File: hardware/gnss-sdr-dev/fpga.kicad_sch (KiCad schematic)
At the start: 31 parts, among them J501 JTAG, J502 LA, U501 LFE5U-25F-6BG256, U502 W25Q128JVSIQ

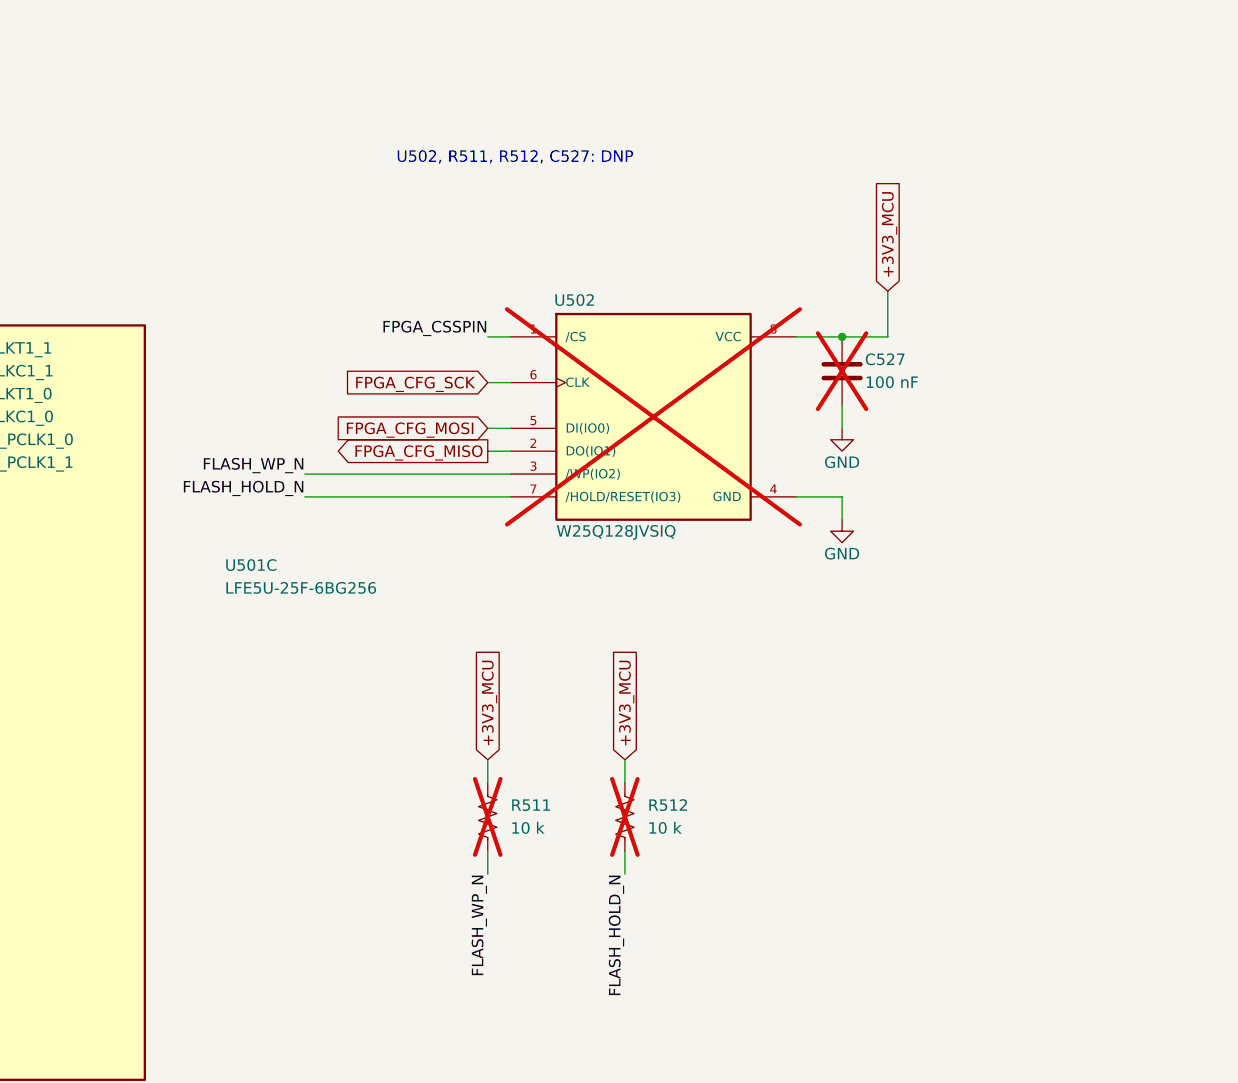
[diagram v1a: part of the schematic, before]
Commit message: hardware(gnss-sdr-dev): U502 becomes the WLCSP W25Q128JVYIQ the P4's boot flash uses, turned 180 deg and routed; the P4 cluster's wiring ripped up for hand routing
P4 rip-up (owner: "rip up the p4 wiring and vias. I'll relocate a bit and do the wiring there by hand"):
- Removed every track and via of the P4's own nets inside the cluster box (124.14, 130.34)-(142.14, 158.23),
  except J5 and R21, plus the dead-end stubs that left outside the box: 953 items.
- Kept the RF section's copper and nets with no pad on a cluster part (VSYS, the USB-C #1 VBUS, J5 CC2).
- VIN from FL401.2 to C402 had looped through the box. It is rerouted locally.

U502, the FPGA configuration flash (DNP: the P4 loads the FPGA):
- Schematic: the W25Q128JVSIQ (SOIC-8) becomes the W25Q128JVYIQ (24-ball WLCSP), the same part and footprint as U7.
  - Same symbol UUID, so the footprint stays linked. Same nets.
  - The 16 unused balls carry no-connect flags.
  - C527 is unchanged (100 nF, DNP, same UUID) and redrawn beside the pull-ups.
- Board: same centre (160.5, 132.6), turned 180 deg.
  - The WLCSP's pinout is mirrored compared with the SOIC's. At 0 deg, WP, MISO and CS (which arrive from the west)
    sit in the ball column whose escape channel faces east, and MOSI, SCK and HOLD the reverse. Every route order left
    one of them boxed in.
  - At 180 deg nothing crosses:
    - MOSI: F.Cu from its BGA escape, south-east past C505, down the east channel.
    - SCK: its In2 lane on south to a via in D2.
    - HOLD: F.Cu out of the east channel's south end to R512.
    - WP: F.Cu out of the west channel's south end to R511.
    - MISO: its F.Cu escape south-west, a via, then B.Cu to a via in C3.
    - CS: In2 from the CSSPIN copper to a via beside B3.
  - +3V3 (B2) and GND (E3) have vias in their pads.
  - The CS via and WP's channel track are placed at fixed points. CS has a 0.259 mm hole gap to C3's via. WP is
    0.15 mm from that via and 0.123 mm from B4.
  - GND return vias sit 1.0 mm from the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
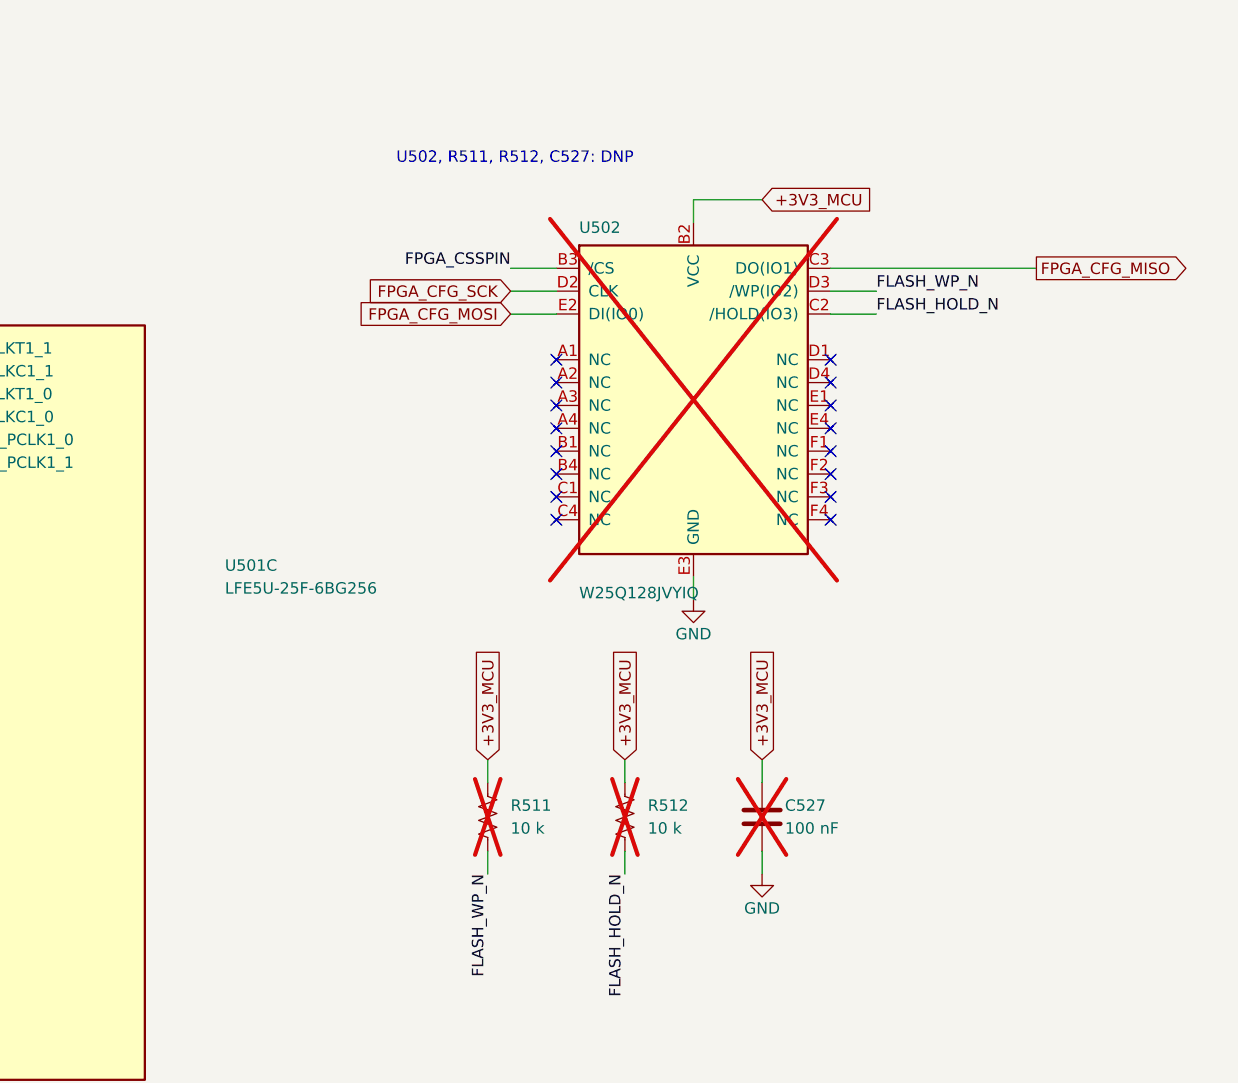
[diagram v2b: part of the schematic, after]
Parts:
- U502: value W25Q128JVSIQ -> W25Q128JVYIQ; footprint Footprints:SOIC127P790X216-8N -> Footprints:24-WLCSP_Y_WIN; symbol Custom:W25Q128JVSIQ -> Custom:W25Q128JVYIQ; MPN W25Q128JVSIQ -> W25Q128JVYIQ
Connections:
- net +3V3_MCU: now also U502.B2 (VCC); no longer U502.8 (VCC)
- net FLASH_HOLD_N: now also U502.C2 (/HOLD(IO3)); no longer U502.7 (/HOLD/RESET(IO3))
- net FLASH_WP_N: now also U502.D3 (/WP(IO2)); no longer U502.3 (/WP(IO2))
- net FPGA_CFG_MISO: now also U502.C3 (DO(IO1)); no longer U502.2 (DO(IO1))
- net FPGA_CFG_MOSI: now also U502.E2 (DI(IO0)); no longer U502.5 (DI(IO0))
- net FPGA_CFG_SCK: now also U502.D2 (CLK); no longer U502.6 (CLK)
- net FPGA_CSSPIN: now also U502.B3 (/CS); no longer U502.1 (/CS)
- net GND: now also U502.E3 (GND); no longer U502.4 (GND)
- no-connect marks 146 -> 162
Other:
- moved on the sheet: C527

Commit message: hardware(gnss-sdr-dev): the design review's before-assembly fixes -- FL401 a 2 A shielded power-line choke, U601 a 0.5 pF HS ESD array with a VBUS TVS, and the value fixes
The boards were not ordered yet, so the copper can still change. Schematic only: the PCB is not updated yet (the
owner runs Update PCB and places FL401, U601 and the new D602), so DRC parity stays red until then.

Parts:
- FL401: Bourns SRF3225TP-501Y (2 A, 0.1 ohm max, 60 V, 500 ohm at 100 MHz, -40 to +105 C, shielded) replaces the
  DLW21SN670HQ2L, a 320 mA USB data-line choke that carried the whole board's input current. No 0805 choke reaches
  0.8 A. New footprint FIL_SRF3225TP (Bourns layout), a CadQuery model and a Custom symbol.
- U601: TI TPD4E05U06DQAR, 0.5 pF. The ESP32-P4 guide allows 1 pF on the high-speed lines; the USBLC6-2SC6 was
  2.5-3.5 pF. USON-10 with D+ on pins 1 and 10 and D- on 2 and 9, for flow-through routing; channel 2 is unused.
- D602 (new): LESD5D5.0CT1G on VBUS_HS, as on Espressif's ESP32-P4-Function-EV-Board. The new U601 has no VBUS pin.
- C403 2.2 -> 22 nF: the GNSS LDO now ramps after the FPGA rails. The front ends no longer drive the ECP5's left
  banks (not hot-socket rated) while those are unpowered.
- R104 10 -> 2.2 ohm: at least 3.15 V at the antenna at 30 mA, and no overload into a shorted feed.
- R503/R504 1 k -> 0 ohm: the configuration straps Lattice asks for (< 500 ohm).
- FB501 470 -> 120 ohm bead (BLM18PG121SN1D), inside the ECP5 checklist's range.
- C105 1 -> 100 nF (the BGA524N6 asks for > 10 nF); C408 1 -> 2.2 uF on the LP5907 output.
- U301 (MAX2771) marked do-not-fit: owner stock, fitted by hand.
- U701's Datasheet field now points at the GD5F2GQ5UE datasheet.
- FABRICATION-NOTES.md: U8 joins the parts with no pin-1 mark, U301 joins the do-not-fit list, and the U9 sentence is
  corrected (U9 makes +3V3_MCU; the FPGA core buck is U403).

ERC: 0 errors and the same 15 warnings. The netlist changes only for the parts above.

The bring-up and firmware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
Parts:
- R503, R504: value 1 k -> 0; MPN RC0402FR-071KL -> RC0402JR-070RL
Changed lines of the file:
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@@
 			)
 		)
-		(property "Value" "1 k"
+		(property "Value" "0"
 			(at 342.9 243.84 0)
 			(show_name no)
@@
 			)
 		)
-		(property "Description" "Resistor 1 k"
+		(property "Description" "Resistor 0"
 			(at 340.36 242.57 0)
 			(hide yes)
@@
 			)
 		)
-		(property "MPN" "RC0402FR-071KL"
+		(property "MPN" "RC0402JR-070RL"
 			(at 340.36 242.57 0)
 			(hide yes)
@@
 			)
 		)
-		(property "Value" "1 k"
+		(property "Value" "0"
 			(at 358.14 246.38 0)
 			(show_name no)
@@
 			)
 		)
-		(property "Description" "Resistor 1 k"
+		(property "Description" "Resistor 0"
 			(at 355.6 245.11 0)
 			(hide yes)
@@
 			)
 		)
-		(property "MPN" "RC0402FR-071KL"
+		(property "MPN" "RC0402JR-070RL"
 			(at 355.6 245.11 0)
 			(hide yes)

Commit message: hardware: the 1 uF 0402 caps consolidate on the 16 V CL05A105KO5NNNC, with the pending part and layout work
Every GRM155R61A105KE15D (Murata, 10 V X5R) becomes the Samsung CL05A105KO5NNNC (16 V X5R) on
space-bug-m8t, gnss-sdr-dev and the legacy gnss-px1105r board -- 34 symbols and their 34 footprints.
Same 0402 footprint, so only the MPN and Mfr change. The higher-rated part is already the 1 uF used
on the Tinker boards, so the BOMs now carry one 1 uF line instead of two.

Pending work committed alongside:
- space-bug-m8t: the 10 uF bulk caps go to CL21A226MOQNNNE, added CL05A106MQ5NUNC, RC0402FR-071KL and
  R-667995 parts, schematic, layout and DRC rule updates, and the new FABRICATION-NOTES.md
- gnss-sdr-dev: the 5.1 nH inductors go from LQG15HS5N1S02D to LQW15AN5N1C00D, added 1 k and 100 k
  resistors, and schematic and layout updates
- legacy gnss-px1105r: the 10 uF caps go to CL21A226MOQNNNE, plus schematic and layout updates
- tinker-beetle: the 390 pF caps go to GRM1555C1H391JA01D, the 100 k resistors to RC0402FR-07100KL,
  and the 2.2 uH inductor from XGL4020-222ME to SRP4020FA-2R2M
- gnss-sam10m8-18mm-hv: the 100 pF cap goes from CL05C101JB5NNNC to GRM1555C1H101JA01D
- the Taoglas CGGBP.25.4.A.02 antenna footprint, and project-file housekeeping

Co-Authored-By: Claude Opus 5.5 <noreply@anthropic.com>
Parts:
- added R516: 1 k, Resistor_SMD:R_0402_1005Metric, symbol Device:R_US
- added R517: 100 k, Resistor_SMD:R_0402_1005Metric, symbol Device:R_US
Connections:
- net EVENT_IN: now also R516.2, R517.1; no longer J502.10 (Pin_10)
- net GND: now also R517.2
- new net EVENT_IN_HDR: J502.10 (Pin_10), R516.1
